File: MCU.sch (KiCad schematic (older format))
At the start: 67 parts, among them J12 USB_B_Mini, J13 Micro_SD_Card, J55 Conn_02x20_Odd_Even, SW1 SW_Push, U1 STM32F407IGTx, U7 24C02, Y1 12MHz, 20pF

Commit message: Added more footprints
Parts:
- BLTouch1: footprint (none) -> Connector_PinHeader_2.54mm:PinHeader_1x04_P2.54mm_Vertical
- L1: footprint (none) -> Inductor_SMD:L_0603_1608Metric_Pad1.05x0.95mm_HandSolder
- R1, R2, R3, R4, R5, R69, R70, R71, R72, R73, R74, R75, R76, R77, R78, R79, R80: footprint (none) -> Resistor_SMD:R_0603_1608Metric_Pad1.05x0.95mm_HandSolder
- SW1: footprint (none) -> Button_Switch_SMD:SW_Push_1P1T_NO_6x6mm_H9.5mm
- Y1: footprint (none) -> Crystal:Crystal_SMD_EuroQuartz_MJ-4Pin_5.0x3.2mm_HandSoldering
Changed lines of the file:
@@
 $Descr A3 16535 11693
 encoding utf-8
-Sheet 4 9
+Sheet 3 9
 Title "MCU"
 Date "2020-10-23"
@@
 F 0 "L1" V 13566 1000 39  0000 C BNN
 F 1 "10uH" V 13491 1000 39  0000 C BNN
-F 2 "" H 13400 1000 50  0001 C CNN
+F 2 "Inductor_SMD:L_0603_1608Metric_Pad1.05x0.95mm_HandSolder" H 13400 1000 50  0001 C CNN
 F 3 "~" H 13400 1000 50  0001 C CNN
 	1    13400 1000
@@
 F 0 "Y1" H 4144 5138 39  0000 C BNN
 F 1 "12MHz, 20pF" V 4144 5063 39  0000 R BNN
-F 2 "" H 3950 5100 50  0001 C CNN
+F 2 "Crystal:Crystal_SMD_EuroQuartz_MJ-4Pin_5.0x3.2mm_HandSoldering" H 3950 5100 50  0001 C CNN
 F 3 "~" H 3950 5100 50  0001 C CNN
 	1    3950 5100
@@
 F 0 "R1" H 4868 1196 50  0000 L CNN
 F 1 "10k" H 4868 1105 50  0000 L CNN
-F 2 "" H 4800 1150 50  0001 C CNN
+F 2 "Resistor_SMD:R_0603_1608Metric_Pad1.05x0.95mm_HandSolder" H 4800 1150 50  0001 C CNN
 F 3 "~" H 4800 1150 50  0001 C CNN
 	1    4800 1150
@@
 F 0 "SW1" V 4846 1552 50  0000 R CNN
 F 1 "SW_Push" V 4755 1552 50  0000 R CNN
-F 2 "" H 4800 1800 50  0001 C CNN
+F 2 "Button_Switch_SMD:SW_Push_1P1T_NO_6x6mm_H9.5mm" H 4800 1800 50  0001 C CNN
 F 3 "~" H 4800 1800 50  0001 C CNN
 	1    4800 1600
@@
 F 0 "R2" V 5450 1250 50  0000 C CNN
 F 1 "1k" V 5450 1450 50  0000 C CNN
-F 2 "" H 5500 1350 50  0001 C CNN
+F 2 "Resistor_SMD:R_0603_1608Metric_Pad1.05x0.95mm_HandSolder" H 5500 1350 50  0001 C CNN
 F 3 "~" H 5500 1350 50  0001 C CNN
 	1    5500 1350
@@
 F 0 "R4" V 6100 2250 50  0000 C CNN
 F 1 "1k" V 6100 2050 50  0000 C CNN
-F 2 "" H 6050 2150 50  0001 C CNN
+F 2 "Resistor_SMD:R_0603_1608Metric_Pad1.05x0.95mm_HandSolder" H 6050 2150 50  0001 C CNN
 F 3 "~" H 6050 2150 50  0001 C CNN
 	1    6050 2150
@@
 F 0 "R3" V 6000 1650 50  0000 C CNN
 F 1 "10k" V 6000 1850 50  0000 C CNN
-F 2 "" H 6050 1750 50  0001 C CNN
+F 2 "Resistor_SMD:R_0603_1608Metric_Pad1.05x0.95mm_HandSolder" H 6050 1750 50  0001 C CNN
 F 3 "~" H 6050 1750 50  0001 C CNN
 	1    6050 1750
@@
 F 0 "R5" V 9745 3250 50  0000 C CNN
 F 1 "10k" V 9836 3250 50  0000 C CNN
-F 2 "" H 9950 3250 50  0001 C CNN
+F 2 "Resistor_SMD:R_0603_1608Metric_Pad1.05x0.95mm_HandSolder" H 9950 3250 50  0001 C CNN
 F 3 "~" H 9950 3250 50  0001 C CNN
 	1    9950 3250
@@
 F 0 "R69" V 2300 2750 50  0000 C CNN
 F 1 "22R" V 2300 2950 50  0000 C CNN
-F 2 "" H 2350 2850 50  0001 C CNN
+F 2 "Resistor_SMD:R_0603_1608Metric_Pad1.05x0.95mm_HandSolder" H 2350 2850 50  0001 C CNN
 F 3 "~" H 2350 2850 50  0001 C CNN
 	1    2350 2850
@@
 F 0 "R70" V 2300 2850 50  0000 C CNN
 F 1 "22R" V 2300 3050 50  0000 C CNN
-F 2 "" H 2350 2950 50  0001 C CNN
+F 2 "Resistor_SMD:R_0603_1608Metric_Pad1.05x0.95mm_HandSolder" H 2350 2950 50  0001 C CNN
 F 3 "~" H 2350 2950 50  0001 C CNN
 	1    2350 2950
@@
 F 0 "R72" V 3950 6500 39  0000 L CNN
 F 1 "10k" V 3950 6300 39  0000 L CNN
-F 2 "" H 3900 6450 50  0001 C CNN
+F 2 "Resistor_SMD:R_0603_1608Metric_Pad1.05x0.95mm_HandSolder" H 3900 6450 50  0001 C CNN
 F 3 "~" H 3900 6450 50  0001 C CNN
 	1    3900 6450
@@
 F 0 "R73" V 4150 6500 39  0000 L CNN
 F 1 "10k" V 4150 6300 39  0000 L CNN
-F 2 "" H 4100 6450 50  0001 C CNN
+F 2 "Resistor_SMD:R_0603_1608Metric_Pad1.05x0.95mm_HandSolder" H 4100 6450 50  0001 C CNN
 F 3 "~" H 4100 6450 50  0001 C CNN
 	1    4100 6450
@@
 F 0 "R71" V 3850 6500 39  0000 L CNN
 F 1 "10k" V 3850 6300 39  0000 L CNN
-F 2 "" H 3800 6450 50  0001 C CNN
+F 2 "Resistor_SMD:R_0603_1608Metric_Pad1.05x0.95mm_HandSolder" H 3800 6450 50  0001 C CNN
 F 3 "~" H 3800 6450 50  0001 C CNN
 	1    3800 6450
@@
 F 0 "R74" V 4250 6500 39  0000 L CNN
 F 1 "10k" V 4250 6300 39  0000 L CNN
-F 2 "" H 4200 6450 50  0001 C CNN
+F 2 "Resistor_SMD:R_0603_1608Metric_Pad1.05x0.95mm_HandSolder" H 4200 6450 50  0001 C CNN
 F 3 "~" H 4200 6450 50  0001 C CNN
 	1    4200 6450
@@
 F 0 "R75" V 4350 6500 39  0000 L CNN
 F 1 "10k" V 4350 6300 39  0000 L CNN
-F 2 "" H 4300 6450 50  0001 C CNN
+F 2 "Resistor_SMD:R_0603_1608Metric_Pad1.05x0.95mm_HandSolder" H 4300 6450 50  0001 C CNN
 F 3 "~" H 4300 6450 50  0001 C CNN
 	1    4300 6450
@@
 F 0 "BLTouch1" H 14030 5242 50  0000 L CNN
 F 1 "Conn_01x04" H 14030 5151 50  0000 L CNN
-F 2 "" H 13950 5250 50  0001 C CNN
+F 2 "Connector_PinHeader_2.54mm:PinHeader_1x04_P2.54mm_Vertical" H 13950 5250 50  0001 C CNN
 F 3 "~" H 13950 5250 50  0001 C CNN
 	1    13950 5250
@@
 F 0 "R78" V 11650 6650 39  0000 L CNN
 F 1 "10k" V 11650 6500 39  0000 L CNN
-F 2 "" H 11600 6600 50  0001 C CNN
+F 2 "Resistor_SMD:R_0603_1608Metric_Pad1.05x0.95mm_HandSolder" H 11600 6600 50  0001 C CNN
 F 3 "~" H 11600 6600 50  0001 C CNN
 	1    11600 6600
@@
 F 0 "R79" V 11800 7400 39  0000 L CNN
 F 1 "10k" V 11800 7250 39  0000 L CNN
-F 2 "" H 11750 7350 50  0001 C CNN
+F 2 "Resistor_SMD:R_0603_1608Metric_Pad1.05x0.95mm_HandSolder" H 11750 7350 50  0001 C CNN
 F 3 "~" H 11750 7350 50  0001 C CNN
 	1    11750 7350
@@
 F 0 "R80" V 11950 6650 39  0000 L CNN
 F 1 "10k" V 11950 6500 39  0000 L CNN
-F 2 "" H 11900 6600 50  0001 C CNN
+F 2 "Resistor_SMD:R_0603_1608Metric_Pad1.05x0.95mm_HandSolder" H 11900 6600 50  0001 C CNN
 F 3 "~" H 11900 6600 50  0001 C CNN
 	1    11900 6600
@@
 F 0 "R76" V 12300 9200 39  0000 L CNN
 F 1 "10k" V 12300 9050 39  0000 L CNN
-F 2 "" H 12250 9150 50  0001 C CNN
+F 2 "Resistor_SMD:R_0603_1608Metric_Pad1.05x0.95mm_HandSolder" H 12250 9150 50  0001 C CNN
 F 3 "~" H 12250 9150 50  0001 C CNN
 	1    12250 9150
@@
 F 0 "R77" V 12450 9200 39  0000 L CNN
 F 1 "10k" V 12450 9050 39  0000 L CNN
-F 2 "" H 12400 9150 50  0001 C CNN
+F 2 "Resistor_SMD:R_0603_1608Metric_Pad1.05x0.95mm_HandSolder" H 12400 9150 50  0001 C CNN
 F 3 "~" H 12400 9150 50  0001 C CNN
 	1    12400 9150

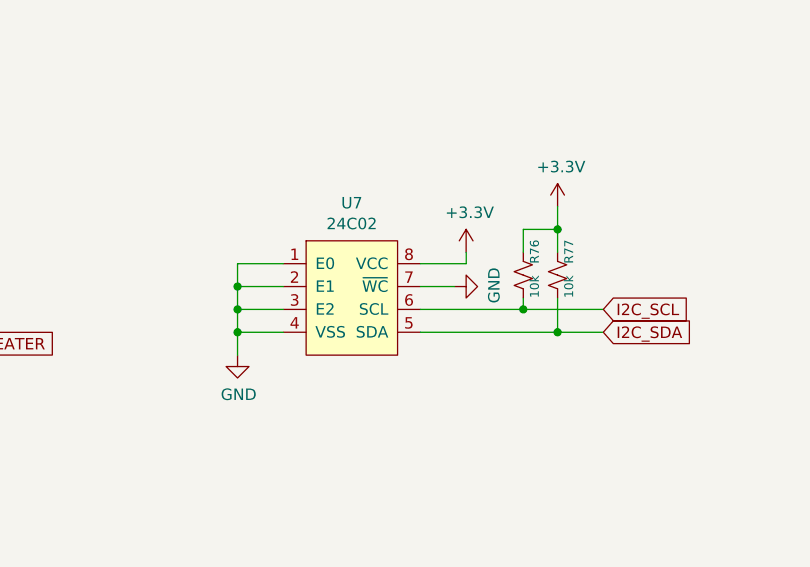
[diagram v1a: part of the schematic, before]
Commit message: finished associating footprints with symbols
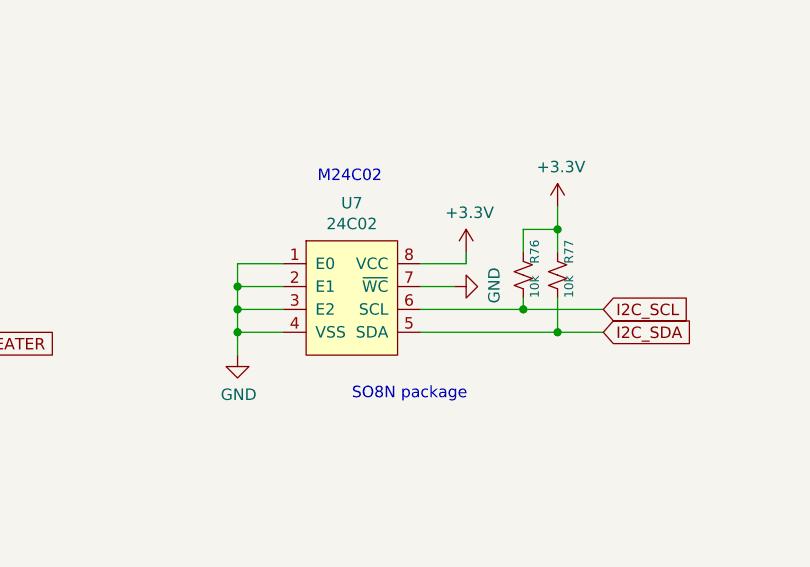
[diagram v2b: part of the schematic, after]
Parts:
- U7: footprint (none) -> Package_SO:SO-8_3.9x4.9mm_P1.27mm
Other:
- note added: "M24C02\n"
- note added: "SO8N package\n"
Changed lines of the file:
@@
 F 0 "U7" H 11500 9665 50  0000 C CNN
 F 1 "24C02" H 11500 9574 50  0000 C CNN
-F 2 "" H 11500 9250 50  0001 C CNN
+F 2 "Package_SO:SO-8_3.9x4.9mm_P1.27mm" H 11500 9250 50  0001 C CNN
 F 3 "" H 11500 9250 50  0001 C CNN
 	1    11500 9250
@@
 NoConn ~ 14950 8350
 NoConn ~ 14950 8450
+Text Notes 11350 8750 0    50   ~ 0
+M24C02\n
+Text Notes 11500 9700 0    50   ~ 0
+SO8N package\n
 $EndSCHEMATC

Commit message: started initial layout
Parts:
- added H1, H2, H3, H4: m4, MountingHole:MountingHole_4.3mm_M4_Pad_Via, symbol Mechanical:MountingHole_Pad
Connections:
- net GND: now also H1.1, H2.1, H3.1, H4.1
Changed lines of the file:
@@
 Text Notes 11500 9700 0    50   ~ 0
 SO8N package\n
+$Comp
+L Mechanical:MountingHole_Pad H1
+U 1 1 5FB94599
+P 2450 9450
+F 0 "H1" H 2550 9499 50  0000 L CNN
+F 1 "m4" H 2550 9408 50  0000 L CNN
+F 2 "MountingHole:MountingHole_4.3mm_M4_Pad_Via" H 2450 9450 50  0001 C CNN
+F 3 "~" H 2450 9450 50  0001 C CNN
+	1    2450 9450
+	1    0    0    -1
+$EndComp
+$Comp
+L power:GND #PWR0255
+U 1 1 5FB956F1
+P 2450 9600
+F 0 "#PWR0255" H 2450 9350 50  0001 C CNN
+F 1 "GND" H 2455 9427 50  0000 C CNN
+F 2 "" H 2450 9600 50  0001 C CNN
+F 3 "" H 2450 9600 50  0001 C CNN
+	1    2450 9600
+	1    0    0    -1
+$EndComp
+Wire Wire Line
+	2450 9600 2450 9550
+$Comp
+L Mechanical:MountingHole_Pad H2
+U 1 1 5FBE19F6
+P 2750 9450
+F 0 "H2" H 2850 9499 50  0000 L CNN
+F 1 "m4" H 2850 9408 50  0000 L CNN
+F 2 "MountingHole:MountingHole_4.3mm_M4_Pad_Via" H 2750 9450 50  0001 C CNN
+F 3 "~" H 2750 9450 50  0001 C CNN
+	1    2750 9450
+	1    0    0    -1
+$EndComp
+$Comp
+L power:GND #PWR0288
+U 1 1 5FBE19FC
+P 2750 9600
+F 0 "#PWR0288" H 2750 9350 50  0001 C CNN
+F 1 "GND" H 2755 9427 50  0000 C CNN
+F 2 "" H 2750 9600 50  0001 C CNN
+F 3 "" H 2750 9600 50  0001 C CNN
+	1    2750 9600
+	1    0    0    -1
+$EndComp
+Wire Wire Line
+	2750 9600 2750 9550
+$Comp
+L Mechanical:MountingHole_Pad H3
+U 1 1 5FC2CD16
+P 3050 9450
+F 0 "H3" H 3150 9499 50  0000 L CNN
+F 1 "m4" H 3150 9408 50  0000 L CNN
+F 2 "MountingHole:MountingHole_4.3mm_M4_Pad_Via" H 3050 9450 50  0001 C CNN
+F 3 "~" H 3050 9450 50  0001 C CNN
+	1    3050 9450
+	1    0    0    -1
+$EndComp
+$Comp
+L power:GND #PWR0289
+U 1 1 5FC2CD1C
+P 3050 9600
+F 0 "#PWR0289" H 3050 9350 50  0001 C CNN
+F 1 "GND" H 3055 9427 50  0000 C CNN
+F 2 "" H 3050 9600 50  0001 C CNN
+F 3 "" H 3050 9600 50  0001 C CNN
+	1    3050 9600
+	1    0    0    -1
+$EndComp
+Wire Wire Line
+	3050 9600 3050 9550
+$Comp
+L Mechanical:MountingHole_Pad H4
+U 1 1 5FC7847A
+P 3350 9450
+F 0 "H4" H 3450 9499 50  0000 L CNN
+F 1 "m4" H 3450 9408 50  0000 L CNN
+F 2 "MountingHole:MountingHole_4.3mm_M4_Pad_Via" H 3350 9450 50  0001 C CNN
+F 3 "~" H 3350 9450 50  0001 C CNN
+	1    3350 9450
+	1    0    0    -1
+$EndComp
+$Comp
+L power:GND #PWR0290
+U 1 1 5FC78480
+P 3350 9600
+F 0 "#PWR0290" H 3350 9350 50  0001 C CNN
+F 1 "GND" H 3355 9427 50  0000 C CNN
+F 2 "" H 3350 9600 50  0001 C CNN
+F 3 "" H 3350 9600 50  0001 C CNN
+	1    3350 9600
+	1    0    0    -1
+$EndComp
+Wire Wire Line
+	3350 9600 3350 9550
 $EndSCHEMATC
